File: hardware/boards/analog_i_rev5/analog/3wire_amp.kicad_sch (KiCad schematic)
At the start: 1 part, among them J12001 Screw_Terminal_01x03

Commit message: clean up new schematic
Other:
- added sheet sallen_key_3kHz (sk_3kHz.kicad_sch)
- note added: "Post-amp active low-pass filter"
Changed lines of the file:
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@@
+	(wire
+		(pts
+			(xy 121.412 81.788) (xy 130.556 81.788)
+		)
+		(stroke
+			(width 0)
+			(type default)
+		)
+	)
 	(wire
 		(pts
@@
 		)
 	)
+	(text "Post-amp active low-pass filter"
+		(exclude_from_sim no)
+		(at 130.556 93.98 0)
+		(effects
+			(font
+				(size 1.27 1.27)
+			)
+			(justify left bottom)
+		)
+	)
 	(hierarchical_label "Vout"
 		(shape input)
-		(at 121.412 81.788 0)
+		(at 148.336 81.788 0)
 		(effects
 			(font
@@
 				)
 			)
+		)
+	)
+	(sheet
+		(at 130.556 76.2)
+		(size 17.78 12.7)
+		(stroke
+			(width 0.1524)
+			(type solid)
+		)
+		(fill
+			(color 0 0 0 0.0000)
+		)
+		(property "Sheetname" "sallen_key_3kHz"
+			(at 132.08 90.678 0)
+			(effects
+				(font
+					(size 1.27 1.27)
+				)
+				(justify left bottom)
+			)
+		)
+		(property "Sheetfile" "sk_3kHz.kicad_sch"
+			(at 130.302 73.914 0)
+			(effects
+				(font
+					(size 1.27 1.27)
+				)
+				(justify left top)
+			)
+		)
+		(pin "VIN" input
+			(at 130.556 81.788 180)
+			(effects
+				(font
+					(size 1.27 1.27)
+				)
+				(justify left)
+			)
+		)
+		(pin "VOUT" input
+			(at 148.336 81.788 0)
+			(effects
+				(font
+					(size 1.27 1.27)
+				)
+				(justify right)
+			)
+		)
+		(instances
+			(project "analog_frontend_panel"
+				(path "/c241d083-1323-4b4a-a540-956d0afb7b72/fb5bb440-61c9-4bd3-9ab6-a463ad90c8bb"
+					(page "15")
+				)
+				(path "/c241d083-1323-4b4a-a540-956d0afb7b72/19141585-7846-417a-91df-f61215fe3233"
+					(page "17")
+				)
+				(path "/c241d083-1323-4b4a-a540-956d0afb7b72/1fbd3e63-3701-4f31-b722-16e65c25cea8"
+					(page "18")
+				)
+			)

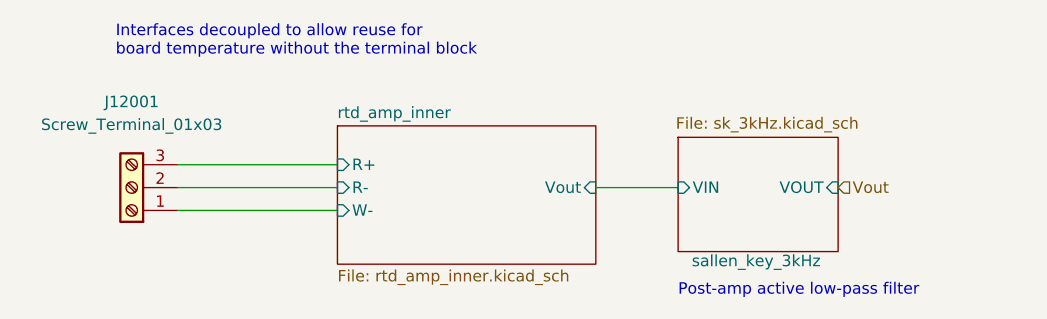
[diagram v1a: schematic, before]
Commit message: finish updating terminals in schematic
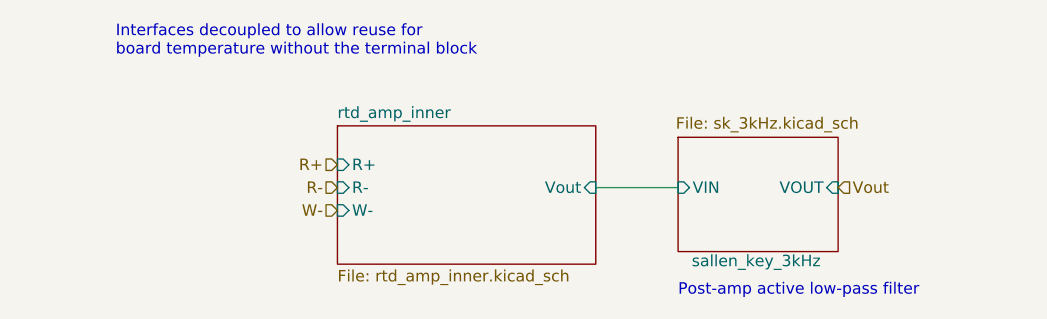
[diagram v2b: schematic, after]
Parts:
- removed J12001: Screw_Terminal_01x03, aaa:Screw_Terminal_3_P5.08mm, symbol Connector:Screw_Terminal_01x03
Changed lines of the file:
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@@
-		)
-	)
-	(wire
-		(pts
-			(xy 74.93 84.328) (xy 92.71 84.328)
-		)
-		(stroke
-			(width 0)
-			(type default)
-		)
-	)
-	(wire
-		(pts
-			(xy 74.93 81.788) (xy 92.71 81.788)
-		)
-		(stroke
-			(width 0)
-			(type default)
-		)
-	)
-	(wire
-		(pts
-			(xy 74.93 79.248) (xy 92.71 79.248)
-		)
-		(stroke
-			(width 0)
-			(type default)
 		)
 	)
@@
 		)
 	)
+	(hierarchical_label "R+"
+		(shape input)
+		(at 92.71 79.248 180)
+		(effects
+			(font
+				(size 1.27 1.27)
+			)
+			(justify right)
+		)
+	)
 	(hierarchical_label "Vout"
 		(shape input)
@@
 		)
 	)
-	(symbol
-		(lib_id "Connector:Screw_Terminal_01x03")
-		(at 69.85 81.788 180)
-		(unit 1)
-		(exclude_from_sim no)
-		(in_bom yes)
-		(on_board yes)
-		(dnp no)
-		(fields_autoplaced yes)
-		(property "Reference" "J12001"
-			(at 69.85 72.263 0)
-			(effects
-				(font
-					(size 1.27 1.27)
-				)
+	(hierarchical_label "R-"
+		(shape input)
+		(at 92.71 81.788 180)
+		(effects
+			(font
+				(size 1.27 1.27)
 			)
-		)
-		(property "Value" "Screw_Terminal_01x03"
-			(at 69.85 74.803 0)
-			(effects
-				(font
-					(size 1.27 1.27)
-				)
-			)
-		)
-		(property "Footprint" "aaa:Screw_Terminal_3_P5.08mm"
-			(at 69.85 81.788 0)
-			(effects
-				(font
-					(size 1.27 1.27)
-				)
-				(hide yes)
-			)
-		)
-		(property "Datasheet" "~"
-			(at 69.85 81.788 0)
-			(effects
-				(font
-					(size 1.27 1.27)
-				)
-				(hide yes)
-			)
-		)
-		(property "Description" ""
-			(at 69.85 81.788 0)
-			(effects
-				(font
-					(size 1.27 1.27)
-				)
-				(hide yes)
-			)
-		)
-		(property "LCSC" "C8270"
-			(at 69.85 81.788 0)
-			(effects
-				(font
-					(size 1.27 1.27)
-				)
-				(hide yes)
-			)
-		)
-		(pin "1"
-		)
-		(pin "2"
-		)
-		(pin "3"
-		)
-		(instances
-			(project "simplicity_analog_1"
-				(path "/5a60c4b1-b6cb-416e-8883-8291fa089b87/c2baf18d-2b19-4edb-98b3-535275ee271f/19141585-7846-417a-91df-f61215fe3233"
-					(reference "J12001")
-					(unit 1)
-				)
-				(path "/5a60c4b1-b6cb-416e-8883-8291fa089b87/c2baf18d-2b19-4edb-98b3-535275ee271f/1fbd3e63-3701-4f31-b722-16e65c25cea8"
-					(reference "J16001")
-					(unit 1)
-				)
-				(path "/5a60c4b1-b6cb-416e-8883-8291fa089b87/c2baf18d-2b19-4edb-98b3-535275ee271f/4491b10b-2044-45ea-b186-c518a135ceee"
-					(reference "J24001")
-					(unit 1)
-				)
-				(path "/5a60c4b1-b6cb-416e-8883-8291fa089b87/c2baf18d-2b19-4edb-98b3-535275ee271f/d6a52a0f-faf0-48a3-a8ea-d9db6b343f24"
-					(reference "J20001")
-					(unit 1)
-				)
-				(path "/5a60c4b1-b6cb-416e-8883-8291fa089b87/c2baf18d-2b19-4edb-98b3-535275ee271f/fb5bb440-61c9-4bd3-9ab6-a463ad90c8bb"
-					(reference "J10001")
-					(unit 1)
-				)
-			)
-			(project "analog_frontend_panel"
-				(path "/c241d083-1323-4b4a-a540-956d0afb7b72/19141585-7846-417a-91df-f61215fe3233"
-					(reference "J9")
-					(unit 1)
-				)
-				(path "/c241d083-1323-4b4a-a540-956d0afb7b72/1fbd3e63-3701-4f31-b722-16e65c25cea8"
-					(reference "J10")
-					(unit 1)
-				)
-				(path "/c241d083-1323-4b4a-a540-956d0afb7b72/fb5bb440-61c9-4bd3-9ab6-a463ad90c8bb"
-					(reference "J8")
-					(unit 1)
-				)
-			)
+			(justify right)
 		)
 	)
+	(hierarchical_label "W-"
+		(shape input)
+		(at 92.71 84.328 180)
+		(effects
+			(font
+				(size 1.27 1.27)
+			)
+			(justify right)
+		)
+	)
